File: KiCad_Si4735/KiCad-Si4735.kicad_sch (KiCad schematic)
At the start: 79 parts, among them J1 I2SOUT, J2 5V, J3 Conn_02x08_Odd_Even, J4 AM/SW, J5 FM, J6 Phone OUT, Q1 3SK291, U1 Si4735-D60-GU, U2 TPA711DR, U3 TPA6111A2DR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

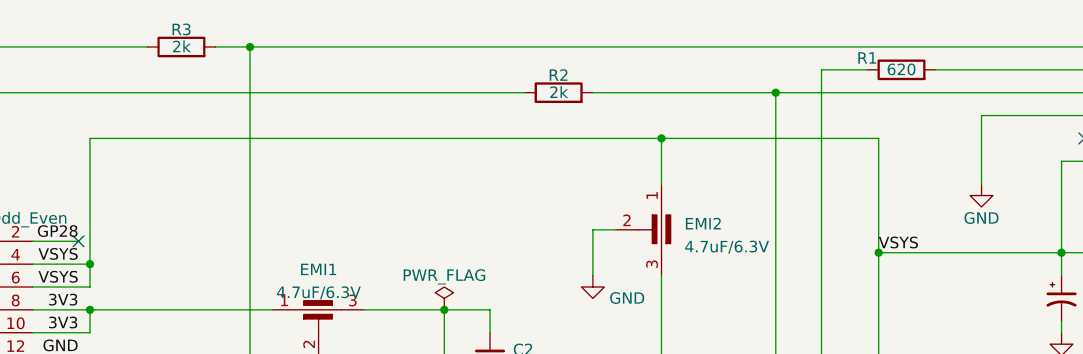
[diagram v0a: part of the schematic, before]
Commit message: change R1, R2, R3 100ohm
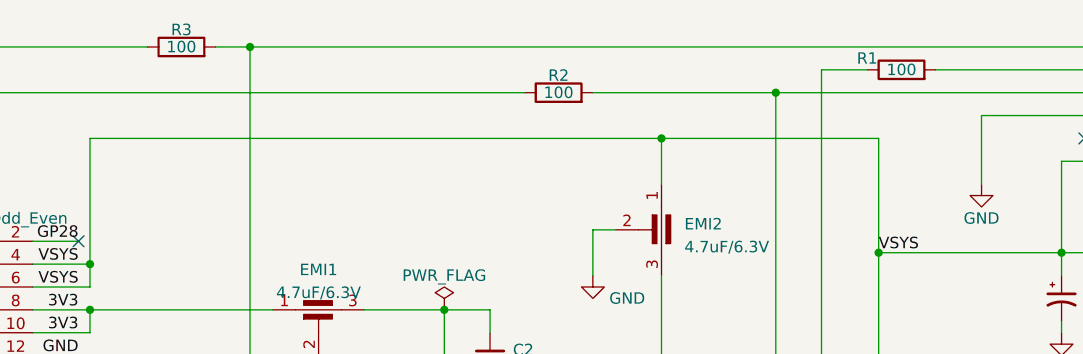
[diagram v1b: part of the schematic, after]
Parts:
- R1: value 620 -> 100
- R2, R3: value 2k -> 100
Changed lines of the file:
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@@
       (effects (font (size 1.27 1.27)))
     )
-    (property "Value" "620" (at 172.72 25.4 90)
+    (property "Value" "100" (at 172.72 25.4 90)
       (effects (font (size 1.27 1.27)))
     )
@@
       (effects (font (size 1.27 1.27)))
     )
-    (property "Value" "2k" (at 92.71 22.86 90)
+    (property "Value" "100" (at 92.71 22.86 90)
       (effects (font (size 1.27 1.27)))
     )
@@
       (effects (font (size 1.27 1.27)))
     )
-    (property "Value" "2k" (at 134.62 27.94 90)
-      (effects (font (size 1.27 1.27)))
-    )
+    (property "Value" "100" (at 134.62 27.94 90)
+      (effects (font (size 1.27 1.27)))
+    )
